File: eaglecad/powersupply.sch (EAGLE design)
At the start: 10 parts

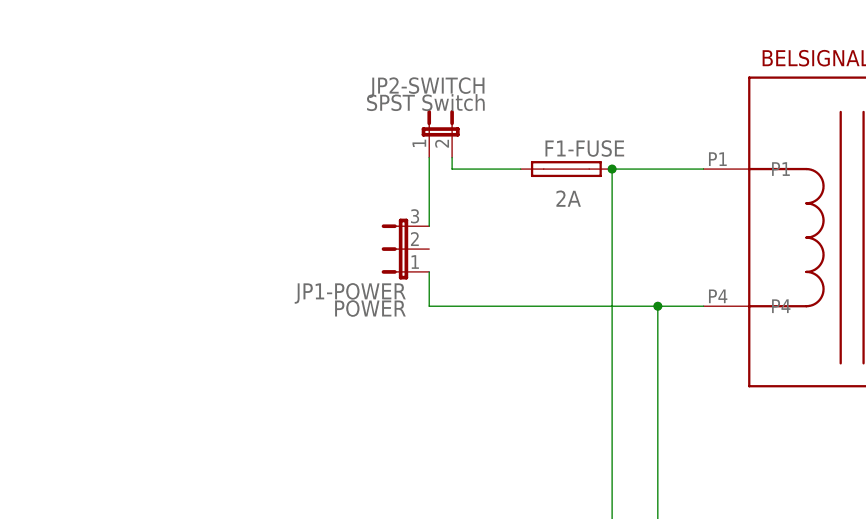
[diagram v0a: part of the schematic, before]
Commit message: changed orientation of fuse and switch on power supply board
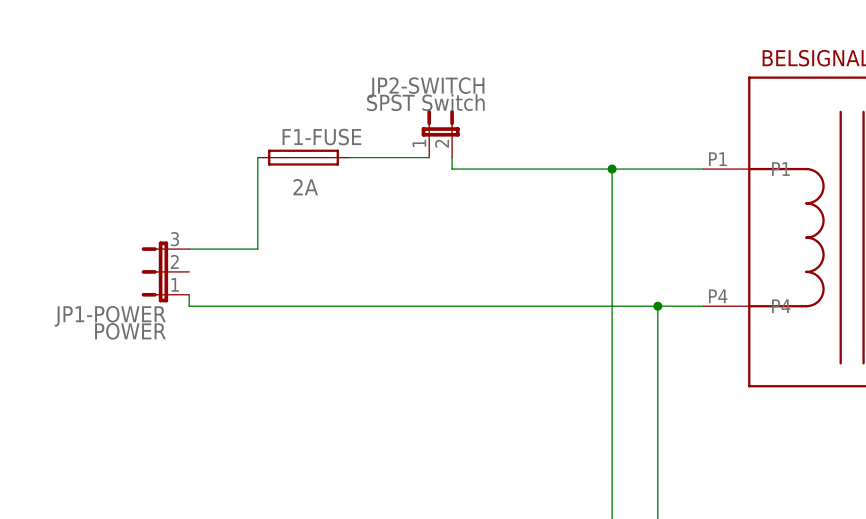
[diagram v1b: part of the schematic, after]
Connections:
- removed net AC-IN-1: JP1-POWER.3, JP2-SWITCH.1
- removed net AC-IN-1-AFTER-FUSE: BELSIGNAL-ST-6-16.P1, F1-FUSE.2, TRIAD-VPP20-1000.P1, TRIAD-VPP20-1000.P4
- removed net AC-IN-2-BEFORE-FUSE: F1-FUSE.1, JP2-SWITCH.2
- new net AC-IN-AFTER-FUSE: F1-FUSE.2, JP2-SWITCH.1
- new net AC-IN-AFTER-SW: BELSIGNAL-ST-6-16.P1, JP2-SWITCH.2, TRIAD-VPP20-1000.P1, TRIAD-VPP20-1000.P4
- new net AC-IN-BEFORE-FUSE: F1-FUSE.1, JP1-POWER.3
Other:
- moved on the sheet: F1-FUSE, JP1-POWER
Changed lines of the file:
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@@
 <setting verticaltext="up"/>
 </settings>
-<grid distance="1.27" unitdist="mm" unit="mm" style="lines" multiple="1" display="no" altdistance="0.127" altunitdist="mm" altunit="mm"/>
+<grid distance="0.05" unitdist="inch" unit="inch" style="lines" multiple="1" display="no" altdistance="0.01" altunitdist="inch" altunit="inch"/>
 <layers>
 <layer number="1" name="Top" color="4" fill="1" visible="no" active="no"/>
@@
 <attribute name="NAME" x="16.51" y="27.94" size="1.778" layer="94"/>
 </instance>
-<instance part="F1-FUSE" gate="1" x="-5.08" y="85.09" smashed="yes">
-<attribute name="NAME" x="-7.62" y="86.487" size="1.778" layer="95"/>
-<attribute name="VALUE" x="-6.35" y="80.899" size="1.778" layer="96"/>
-</instance>
-<instance part="JP1-POWER" gate="1" x="-22.86" y="76.2" smashed="yes" rot="R90">
-<attribute name="NAME" x="-22.86" y="72.39" size="1.778" layer="95" rot="R180"/>
-<attribute name="VALUE" x="-22.86" y="70.485" size="1.778" layer="96" rot="R180"/>
+<instance part="F1-FUSE" gate="1" x="-34.29" y="86.36" smashed="yes">
+<attribute name="NAME" x="-36.83" y="87.757" size="1.778" layer="95"/>
+<attribute name="VALUE" x="-35.56" y="82.169" size="1.778" layer="96"/>
+</instance>
+<instance part="JP1-POWER" gate="1" x="-49.53" y="73.66" smashed="yes" rot="R90">
+<attribute name="NAME" x="-49.53" y="69.85" size="1.778" layer="95" rot="R180"/>
+<attribute name="VALUE" x="-49.53" y="67.945" size="1.778" layer="96" rot="R180"/>
 </instance>
 <instance part="JP2-SWITCH" gate="A" x="-20.32" y="88.9" smashed="yes">
@@
 <wire x1="5.08" y1="20.32" x2="5.08" y2="69.85" width="0.1524" layer="91"/>
 <junction x="5.08" y="20.32"/>
-<pinref part="JP1-POWER" gate="1" pin="1"/>
-<wire x1="5.08" y1="69.85" x2="-20.32" y2="69.85" width="0.1524" layer="91"/>
-<wire x1="-20.32" y1="69.85" x2="-20.32" y2="73.66" width="0.1524" layer="91"/>
 <pinref part="BELSIGNAL-ST-6-16" gate="G$1" pin="P4"/>
 <wire x1="10.16" y1="69.85" x2="5.08" y2="69.85" width="0.1524" layer="91"/>
+<pinref part="JP1-POWER" gate="1" pin="1"/>
+<wire x1="5.08" y1="69.85" x2="-46.99" y2="69.85" width="0.1524" layer="91"/>
+<wire x1="-46.99" y1="69.85" x2="-46.99" y2="71.12" width="0.1524" layer="91"/>
 <junction x="5.08" y="69.85"/>
-</segment>
-</net>
-<net name="AC-IN-1" class="0">
-<segment>
-<pinref part="JP1-POWER" gate="1" pin="3"/>
-<pinref part="JP2-SWITCH" gate="A" pin="1"/>
-<wire x1="-20.32" y1="78.74" x2="-20.32" y2="86.36" width="0.1524" layer="91"/>
 </segment>
 </net>
@@
 <wire x1="106.68" y1="38.1" x2="114.3" y2="38.1" width="0.1524" layer="91"/>
 <junction x="114.3" y="38.1"/>
-</segment>
-</net>
-<net name="AC-IN-1-AFTER-FUSE" class="0">
-<segment>
-<pinref part="F1-FUSE" gate="1" pin="2"/>
-<pinref part="TRIAD-VPP20-1000" gate="G$1" pin="P4"/>
-<wire x1="0" y1="85.09" x2="10.16" y2="85.09" width="0.1524" layer="91"/>
-<wire x1="10.16" y1="10.16" x2="0" y2="10.16" width="0.1524" layer="91"/>
-<wire x1="0" y1="10.16" x2="0" y2="25.4" width="0.1524" layer="91"/>
-<pinref part="TRIAD-VPP20-1000" gate="G$1" pin="P1"/>
-<wire x1="0" y1="25.4" x2="10.16" y2="25.4" width="0.1524" layer="91"/>
-<wire x1="0" y1="25.4" x2="0" y2="85.09" width="0.1524" layer="91"/>
-<junction x="0" y="25.4"/>
-<junction x="0" y="85.09"/>
-<pinref part="BELSIGNAL-ST-6-16" gate="G$1" pin="P1"/>
 </segment>
 </net>
@@
 </segment>
 </net>
-<net name="AC-IN-2-BEFORE-FUSE" class="0">
+<net name="AC-IN-AFTER-SW" class="0">
+<segment>
+<pinref part="JP2-SWITCH" gate="A" pin="2"/>
+<pinref part="TRIAD-VPP20-1000" gate="G$1" pin="P4"/>
+<wire x1="10.16" y1="10.16" x2="0" y2="10.16" width="0.1524" layer="91"/>
+<wire x1="0" y1="10.16" x2="0" y2="25.4" width="0.1524" layer="91"/>
+<pinref part="TRIAD-VPP20-1000" gate="G$1" pin="P1"/>
+<wire x1="0" y1="25.4" x2="10.16" y2="25.4" width="0.1524" layer="91"/>
+<wire x1="0" y1="25.4" x2="0" y2="85.09" width="0.1524" layer="91"/>
+<junction x="0" y="25.4"/>
+<pinref part="BELSIGNAL-ST-6-16" gate="G$1" pin="P1"/>
+<wire x1="10.16" y1="85.09" x2="0" y2="85.09" width="0.1524" layer="91"/>
+<wire x1="-17.78" y1="86.36" x2="-17.78" y2="85.09" width="0.1524" layer="91"/>
+<wire x1="-17.78" y1="85.09" x2="0" y2="85.09" width="0.1524" layer="91"/>
+<junction x="0" y="85.09"/>
+</segment>
+</net>
+<net name="AC-IN-AFTER-FUSE" class="0">
+<segment>
+<pinref part="JP2-SWITCH" gate="A" pin="1"/>
+<pinref part="F1-FUSE" gate="1" pin="2"/>
+<wire x1="-20.32" y1="86.36" x2="-29.21" y2="86.36" width="0.1524" layer="91"/>
+</segment>
+</net>
+<net name="AC-IN-BEFORE-FUSE" class="0">
 <segment>
 <pinref part="F1-FUSE" gate="1" pin="1"/>
-<pinref part="JP2-SWITCH" gate="A" pin="2"/>
-<wire x1="-10.16" y1="85.09" x2="-17.78" y2="85.09" width="0.1524" layer="91"/>
-<wire x1="-17.78" y1="85.09" x2="-17.78" y2="86.36" width="0.1524" layer="91"/>
-</segment>
-</net>
+<pinref part="JP1-POWER" gate="1" pin="3"/>
+<wire x1="-39.37" y1="86.36" x2="-39.37" y2="76.2" width="0.1524" layer="91"/>
+<wire x1="-39.37" y1="76.2" x2="-46.99" y2="76.2" width="0.1524" layer="91"/>
+</segment>
+</net>
